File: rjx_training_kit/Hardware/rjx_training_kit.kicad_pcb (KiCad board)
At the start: 4 copper layers, 91.4 x 94.3 mm, 110 parts, among them J1 Barrel_Jack_Switch, J2 Conn_01x32_Pin, J3 Conn_01x32_Pin, J4 LiPo_4.2V, J5 LiPo_4.2V, J6 CHG_OUT, J7 CAN_Bus, J8 CAN_Bus, J9 Conn_01x03_Pin, Q1 BC817, Q2 BC817, Q3 BC817, Q4 BC808, Q5 BC817, SW1 SW_Push, SW2 SW_Push, U1 TLV76133DCY, U2 LD39200DPUR, U3 BQ24072RGT, U4 LIS3DH, U5 BQ27441-G1, U6 KCSA02-136, U7 TMP1075DGK, U8 MCP2562-E-SN, U9 STM32L431RCTx, Y1 8MHz

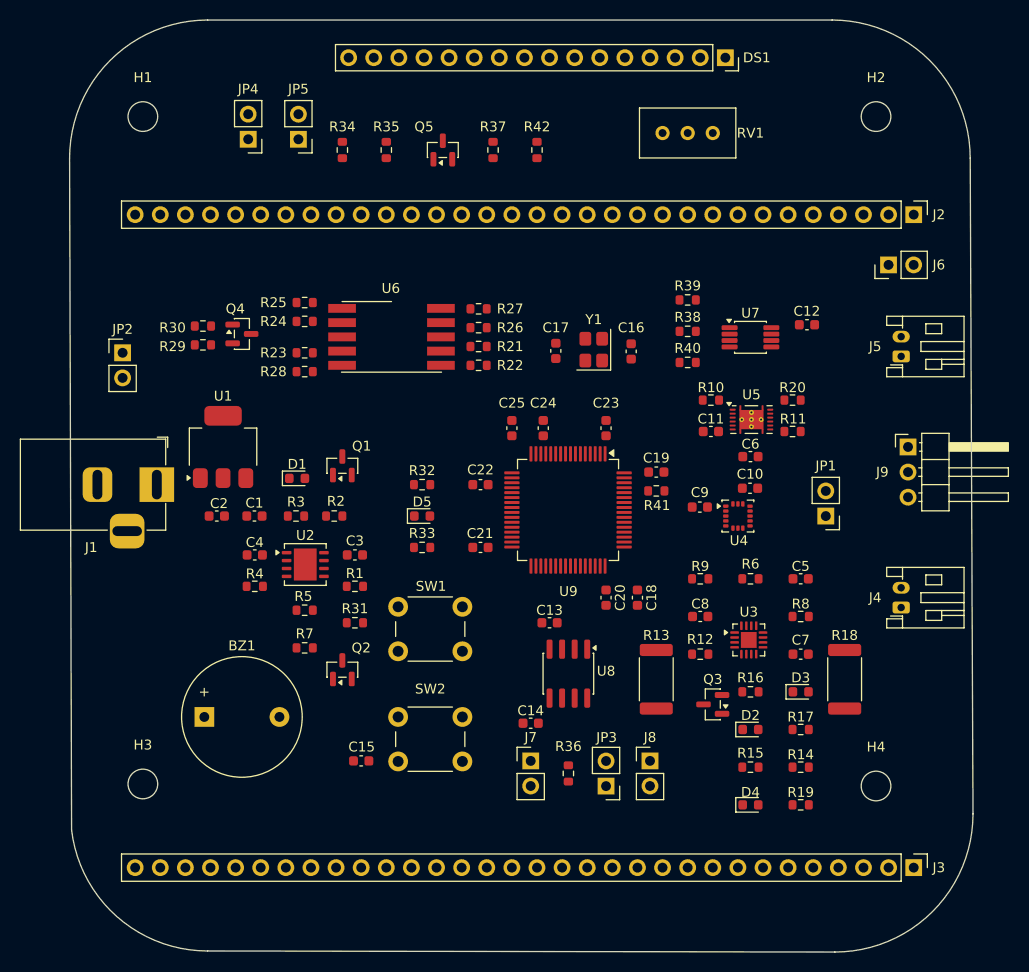
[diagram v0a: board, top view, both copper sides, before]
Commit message: [RJX]: Improved component placement.
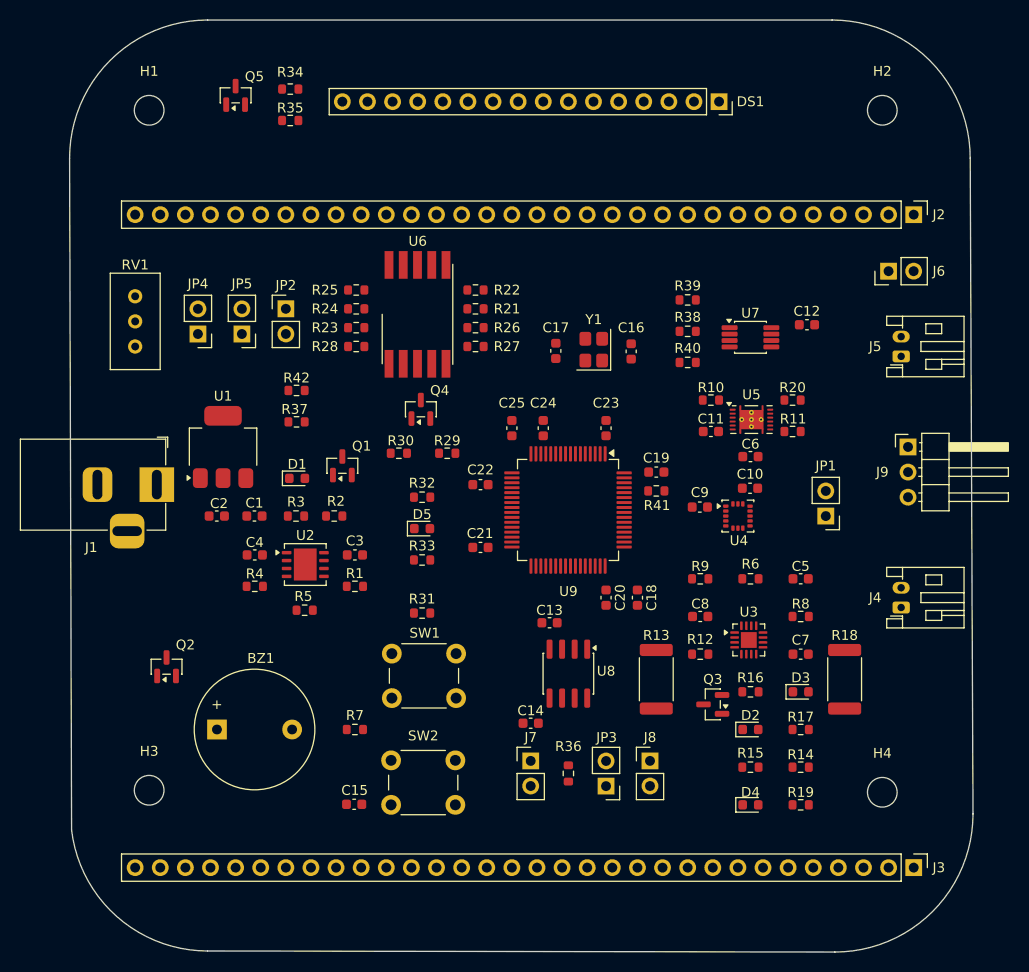
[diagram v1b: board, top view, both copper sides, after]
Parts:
- moved RV1 55.8 mm to (45.7, 66.7), turned to 90 degrees
- moved R42 34.4 mm to (62.0, 76.2), turned to 0 degrees
- moved R37 33.9 mm to (62.0, 79.4), turned to 0 degrees
- moved R29 27.0 mm to (77.3, 82.5)
- moved R30 23.6 mm to (72.4, 82.5), turned to 180 degrees
- moved Q5 21.7 mm to (55.9, 46.4)
- moved JP5 20.5 mm to (56.5, 70.5)
- moved JP4 20.3 mm to (52.1, 70.5)
- moved Q4 19.6 mm to (74.6, 78.1), turned to 90 degrees
- moved Q2 17.8 mm to (48.9, 104.1)
- moved JP2 17.1 mm to (61.0, 67.9)
- moved R35 10.2 mm to (61.4, 48.9), turned to 0 degrees
- moved R7 9.69 mm to (67.9, 110.5)
- moved R34 8.11 mm to (61.4, 45.7), turned to 180 degrees
- moved R22 7.63 mm to (80.1, 66.0)
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
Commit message: [RJX]: Added silkscreen for pin headers and connectors.
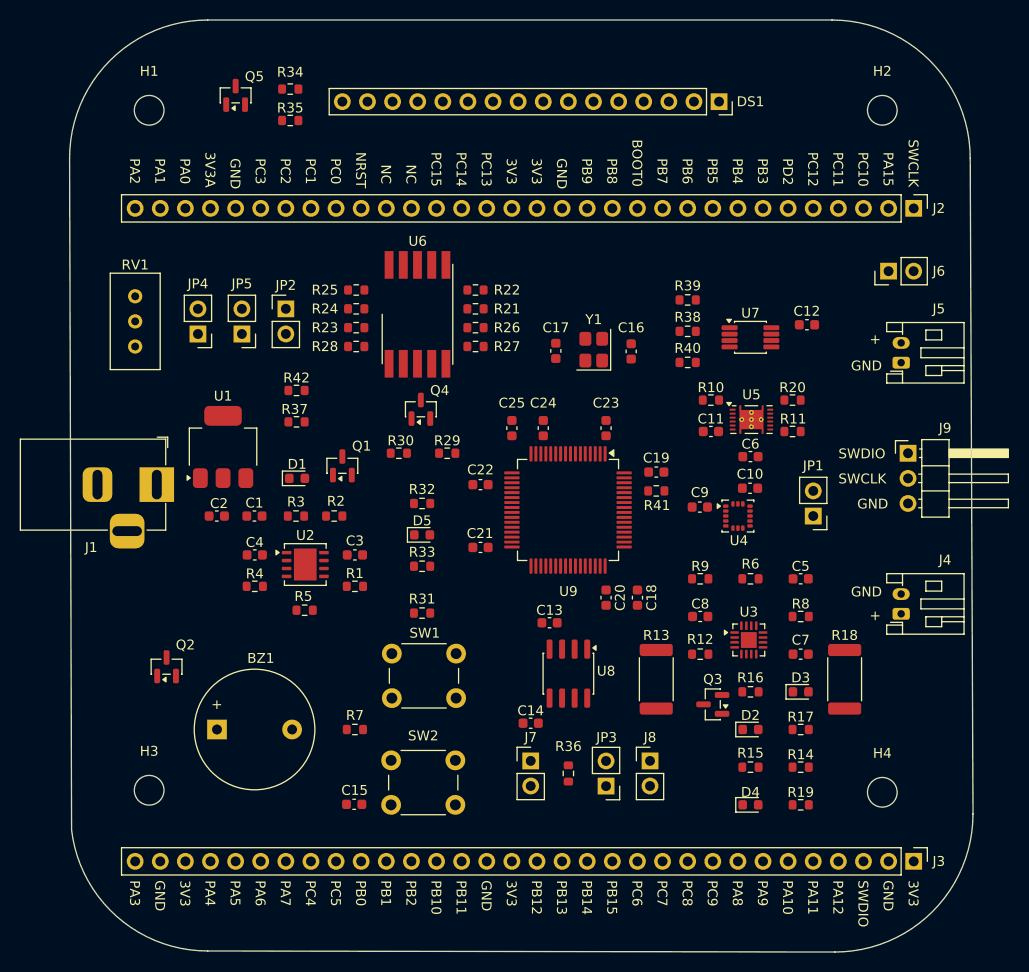
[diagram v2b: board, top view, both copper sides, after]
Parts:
- moved JP1 1.27 mm to (114.3, 88.9)
- moved D5 0.64 mm to (74.7, 90.8)
- moved J2 0.64 mm to (124.5, 57.8)
- moved J4 0.64 mm to (123.2, 98.8)
- moved J5 0.64 mm to (123.2, 73.4)
- moved R33 0.64 mm to (74.7, 94.0)
- moved J3 0.63 mm to (124.5, 123.8)
- moved J9 0.63 mm to (123.9, 82.5)
- moved R32 0.63 mm to (74.7, 87.6)
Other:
- board text added: "+"
- board text added: "3V3"
- board text added: "3V3A"
- board text added: "BOOT0"
- board text added: "GND"
- board text added: "NC"
- board text added: "NRST"
- board text added: "PA0"
- board text added: "PA1"
- board text added: "PA10"
- board text added: "PA11"
- board text added: "PA12"
- board text added: "PA15"
- board text added: "PA2"
- board text added: "PA3"
- board text added: "PA4"
- board text added: "PA5"
- board text added: "PA6"
- board text added: "PA7"
- board text added: "PA8"
- board text added: "PA9"
- board text added: "PB0"
- board text added: "PB1"
- board text added: "PB10"
- board text added: "PB11"
- board text added: "PB12"
- board text added: "PB13"
- board text added: "PB14"
- board text added: "PB15"
- board text added: "PB2"
- board text added: "PB3"
- board text added: "PB4"
- board text added: "PB5"
- board text added: "PB6"
- board text added: "PB7"
- board text added: "PB8"
- board text added: "PB9"
- board text added: "PC0"
- board text added: "PC1"
- board text added: "PC10"
- board text added: "PC11"
- board text added: "PC12"
- board text added: "PC13"
- board text added: "PC14"
- board text added: "PC15"
- board text added: "PC2"
- board text added: "PC3"
- board text added: "PC4"
- board text added: "PC5"
- board text added: "PC6"
- board text added: "PC7"
- board text added: "PC8"
- board text added: "PC9"
- board text added: "PD2"
- board text added: "SWCLK"
- board text added: "SWDIO"

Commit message: [RJX]: Resolved DRC errors due to aggressive board setup configurations.
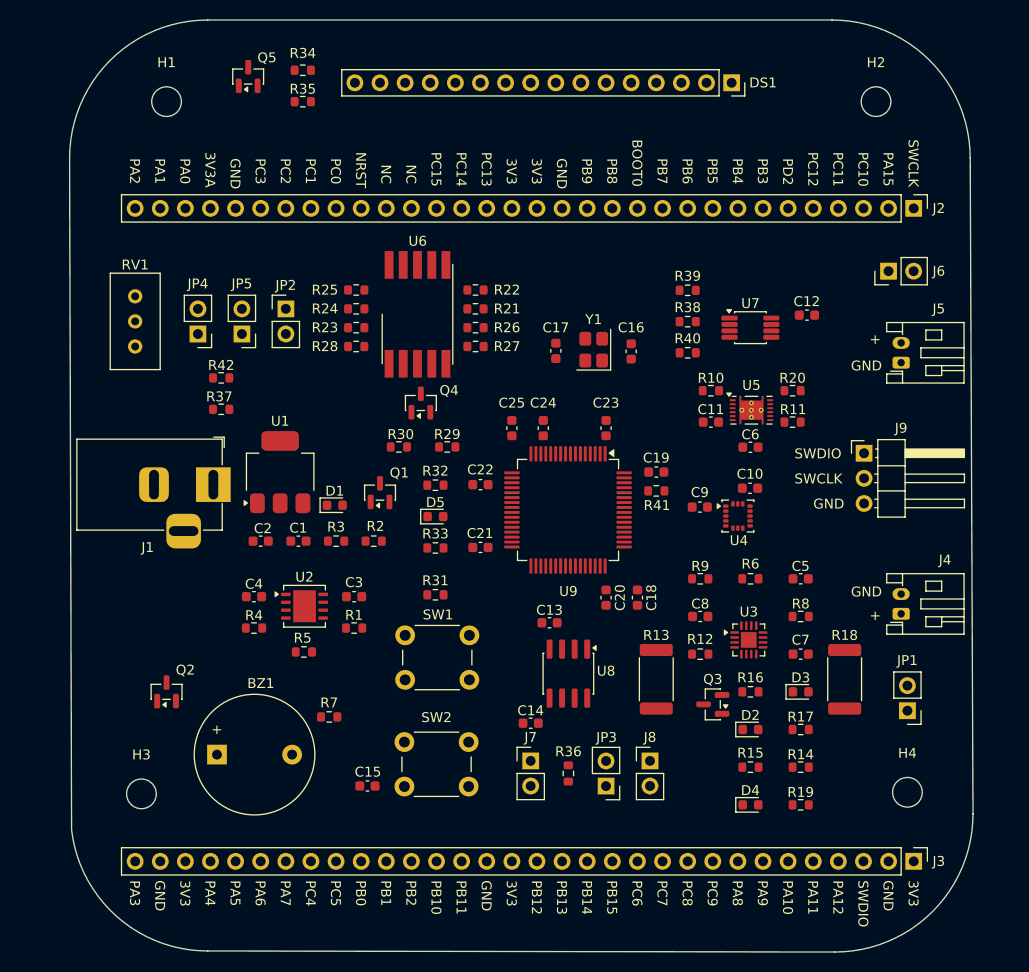
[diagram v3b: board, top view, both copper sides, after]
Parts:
- moved JP1 21.9 mm to (123.8, 108.6)
- moved R37 7.73 mm to (54.4, 78.1)
- moved R42 7.73 mm to (54.4, 74.9)
- moved U1 6.31 mm to (60.4, 84.5)
- moved J1 5.72 mm to (53.6, 85.7)
- moved C1 5.12 mm to (62.2, 91.4)
- moved C2 5.12 mm to (58.4, 91.4)
- moved R3 4.78 mm to (66.0, 91.4)
- moved R2 4.74 mm to (69.8, 91.4)
- moved D1 4.68 mm to (65.9, 87.8)
- moved Q1 4.68 mm to (70.5, 86.5)
- moved J9 4.45 mm to (119.4, 82.5)
- moved C3 4.22 mm to (67.9, 97.1)
- moved C4 4.22 mm to (57.7, 97.1)
- moved R1 4.22 mm to (67.9, 100.2)
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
